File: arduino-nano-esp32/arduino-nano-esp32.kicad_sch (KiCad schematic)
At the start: 1 part

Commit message: symbol lib
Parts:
- added RFM95W1: ~, maciek-lib:lora-adafruit, symbol maciek-symbols:adafruit-rfm95w
- added SW1, SW2: ~, maciek-lib:3x4 switch, symbol maciek-symbols:3x4_switch
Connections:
- net +3.3V: now also RFM95W1.9 (VIN)
- net GND: now also RFM95W1.8 (GND), SW1.2, SW2.1
- net at A1.B1: now also SW1.1
- net at A1.D2: now also SW2.2
- net at A1.D3: now also RFM95W1.1
- net at A1.D4: now also RFM95W1.2
- net at A1.D5: now also RFM95W1.3
- net at A1.D6: now also RFM95W1.4
- net at A1.D7: now also RFM95W1.5
- net at A1.D8: now also RFM95W1.6
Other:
- moved on the sheet: A1

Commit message: net class plus cleanup
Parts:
- RFM95W1: footprint maciek-lib:lora-adafruit -> lora-adafruit
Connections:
- no-connect marks 0 -> 28
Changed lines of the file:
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@@
 		(color 0 0 0 0)
 	)
+	(no_connect
+		(at 143.51 59.69)
+	)
+	(no_connect
+		(at 113.03 40.64)
+	)
+	(no_connect
+		(at 97.79 66.04)
+	)
+	(no_connect
+		(at 46.99 93.98)
+	)
+	(no_connect
+		(at 46.99 81.28)
+	)
+	(no_connect
+		(at 143.51 62.23)
+	)
+	(no_connect
+		(at 97.79 53.34)
+	)
+	(no_connect
+		(at 113.03 121.92)
+	)
+	(no_connect
+		(at 97.79 71.12)
+	)
+	(no_connect
+		(at 46.99 66.04)
+	)
+	(no_connect
+		(at 46.99 71.12)
+	)
+	(no_connect
+		(at 123.19 64.77)
+	)
+	(no_connect
+		(at 97.79 68.58)
+	)
+	(no_connect
+		(at 97.79 73.66)
+	)
+	(no_connect
+		(at 97.79 55.88)
+	)
+	(no_connect
+		(at 97.79 76.2)
+	)
+	(no_connect
+		(at 46.99 68.58)
+	)
+	(no_connect
+		(at 143.51 69.85)
+	)
+	(no_connect
+		(at 143.51 64.77)
+	)
+	(no_connect
+		(at 143.51 67.31)
+	)
+	(no_connect
+		(at 46.99 78.74)
+	)
+	(no_connect
+		(at 46.99 83.82)
+	)
+	(no_connect
+		(at 46.99 73.66)
+	)
+	(no_connect
+		(at 113.03 111.76)
+	)
+	(no_connect
+		(at 46.99 91.44)
+	)
+	(no_connect
+		(at 46.99 58.42)
+	)
+	(no_connect
+		(at 46.99 76.2)
+	)
+	(no_connect
+		(at 113.03 50.8)
+	)
 	(wire
 		(pts
@@
 			(width 0)
 			(type default)
+		)
+	)
+	(netclass_flag ""
+		(length 2.54)
+		(shape round)
+		(at 33.02 105.41 90)
+		(fields_autoplaced yes)
+		(effects
+			(font
+				(size 1.27 1.27)
+			)
+			(justify left bottom)
+		)
+		(property "Netclass" "POWER"
+			(at 30.48 104.7115 90)
+			(effects
+				(font
+					(size 1.27 1.27)
+					(italic yes)
+				)
+				(justify left)
+			)
+		)
+	)
+	(netclass_flag ""
+		(length 2.54)
+		(shape round)
+		(at 25.4 44.45 90)
+		(fields_autoplaced yes)
+		(effects
+			(font
+				(size 1.27 1.27)
+			)
+			(justify left bottom)
+		)
+		(property "Netclass" "POWER"
+			(at 22.86 43.7515 90)
+			(effects
+				(font
+					(size 1.27 1.27)
+					(italic yes)
+				)
+				(justify left)
+			)
 		)
 	)
@@
 			)
 		)
-		(property "Footprint" "maciek-lib:lora-adafruit"
+		(property "Footprint" "lora-adafruit"
 			(at 142.24 80.01 0)
 			(effects

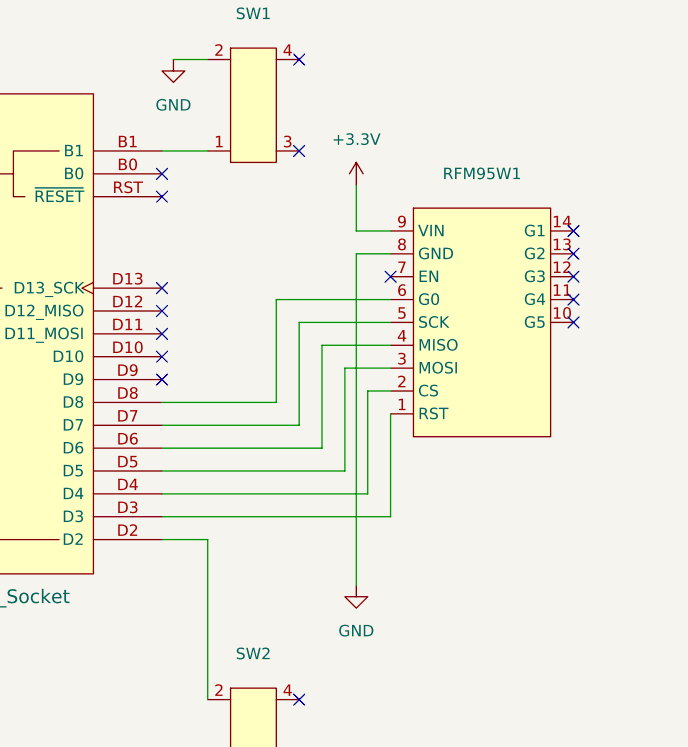
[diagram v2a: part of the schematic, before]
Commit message: add nests and 3v3 area
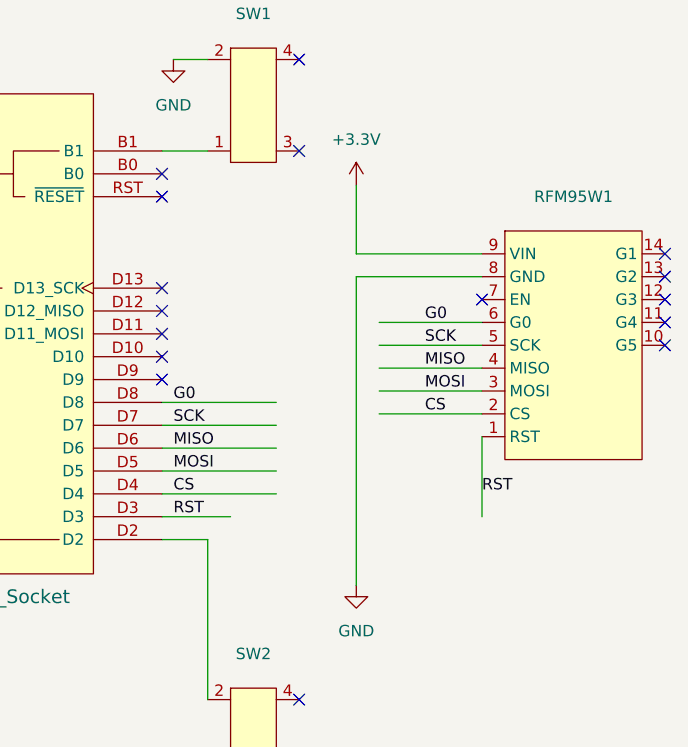
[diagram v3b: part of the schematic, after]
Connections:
- net RST: now reaches A1.D3, RFM95W1.1 (RST)
- net CS: now reaches A1.D4, RFM95W1.2 (CS)
- net MOSI: now reaches A1.D5, RFM95W1.3 (MOSI)
- net MISO: now reaches A1.D6, RFM95W1.4 (MISO)
- net SCK: now reaches A1.D7, RFM95W1.5 (SCK)
- net G0: now reaches A1.D8, RFM95W1.6 (G0)
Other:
- moved on the sheet: RFM95W1
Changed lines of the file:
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@@
 	)
 	(no_connect
-		(at 143.51 59.69)
+		(at 153.67 62.23)
 	)
 	(no_connect
@@
 	)
 	(no_connect
-		(at 143.51 62.23)
+		(at 153.67 64.77)
 	)
 	(no_connect
@@
 	)
 	(no_connect
-		(at 123.19 64.77)
+		(at 133.35 67.31)
 	)
 	(no_connect
@@
 	)
 	(no_connect
-		(at 143.51 69.85)
-	)
-	(no_connect
-		(at 143.51 64.77)
-	)
-	(no_connect
-		(at 143.51 67.31)
+		(at 153.67 72.39)
+	)
+	(no_connect
+		(at 153.67 67.31)
+	)
+	(no_connect
+		(at 153.67 69.85)
 	)
 	(no_connect
@@
 	(wire
 		(pts
-			(xy 110.49 67.31) (xy 123.19 67.31)
+			(xy 121.92 69.85) (xy 133.35 69.85)
 		)
 		(stroke
@@
 	(wire
 		(pts
-			(xy 97.79 81.28) (xy 113.03 81.28)
-		)
-		(stroke
-			(width 0)
-			(type default)
-		)
-	)
-	(wire
-		(pts
-			(xy 115.57 83.82) (xy 115.57 72.39)
+			(xy 97.79 81.28) (xy 110.49 81.28)
 		)
 		(stroke
@@
 	(wire
 		(pts
-			(xy 97.79 91.44) (xy 123.19 91.44)
-		)
-		(stroke
-			(width 0)
-			(type default)
-		)
-	)
-	(wire
-		(pts
-			(xy 118.11 86.36) (xy 118.11 74.93)
-		)
-		(stroke
-			(width 0)
-			(type default)
-		)
-	)
-	(wire
-		(pts
 			(xy 102.87 93.98) (xy 97.79 93.98)
 		)
@@
 	(wire
 		(pts
-			(xy 123.19 91.44) (xy 123.19 80.01)
-		)
-		(stroke
-			(width 0)
-			(type default)
-		)
-	)
-	(wire
-		(pts
-			(xy 110.49 78.74) (xy 110.49 67.31)
-		)
-		(stroke
-			(width 0)
-			(type default)
-		)
-	)
-	(wire
-		(pts
 			(xy 33.02 48.26) (xy 46.99 48.26)
 		)
@@
 	(wire
 		(pts
-			(xy 119.38 62.23) (xy 119.38 99.06)
-		)
-		(stroke
-			(width 0)
-			(type default)
-		)
-	)
-	(wire
-		(pts
-			(xy 113.03 69.85) (xy 123.19 69.85)
+			(xy 119.38 64.77) (xy 119.38 99.06)
+		)
+		(stroke
+			(width 0)
+			(type default)
+		)
+	)
+	(wire
+		(pts
+			(xy 121.92 72.39) (xy 133.35 72.39)
 		)
 		(stroke
@@
 	(wire
 		(pts
-			(xy 97.79 88.9) (xy 120.65 88.9)
+			(xy 97.79 88.9) (xy 110.49 88.9)
 		)
 		(stroke
@@
 	(wire
 		(pts
-			(xy 119.38 59.69) (xy 119.38 54.61)
+			(xy 119.38 62.23) (xy 119.38 54.61)
 		)
 		(stroke
@@
 	(wire
 		(pts
-			(xy 97.79 83.82) (xy 115.57 83.82)
-		)
-		(stroke
-			(width 0)
-			(type default)
-		)
-	)
-	(wire
-		(pts
-			(xy 113.03 81.28) (xy 113.03 69.85)
-		)
-		(stroke
-			(width 0)
-			(type default)
-		)
-	)
-	(wire
-		(pts
-			(xy 120.65 77.47) (xy 123.19 77.47)
-		)
-		(stroke
-			(width 0)
-			(type default)
-		)
-	)
-	(wire
-		(pts
-			(xy 115.57 72.39) (xy 123.19 72.39)
-		)
-		(stroke
-			(width 0)
-			(type default)
-		)
-	)
-	(wire
-		(pts
-			(xy 120.65 88.9) (xy 120.65 77.47)
-		)
-		(stroke
-			(width 0)
-			(type default)
-		)
-	)
-	(wire
-		(pts
-			(xy 118.11 74.93) (xy 123.19 74.93)
+			(xy 97.79 83.82) (xy 110.49 83.82)
+		)
+		(stroke
+			(width 0)
+			(type default)
+		)
+	)
+	(wire
+		(pts
+			(xy 121.92 80.01) (xy 133.35 80.01)
+		)
+		(stroke
+			(width 0)
+			(type default)
+		)
+	)
+	(wire
+		(pts
+			(xy 121.92 74.93) (xy 133.35 74.93)
+		)
+		(stroke
+			(width 0)
+			(type default)
+		)
+	)
+	(wire
+		(pts
+			(xy 121.92 77.47) (xy 133.35 77.47)
 		)
 		(stroke
@@
 	(wire
 		(pts
-			(xy 123.19 62.23) (xy 119.38 62.23)
-		)
-		(stroke
-			(width 0)
-			(type default)
-		)
-	)
-	(wire
-		(pts
-			(xy 97.79 86.36) (xy 118.11 86.36)
-		)
-		(stroke
-			(width 0)
-			(type default)
-		)
-	)
-	(wire
-		(pts
-			(xy 123.19 59.69) (xy 119.38 59.69)
+			(xy 133.35 91.44) (xy 133.35 82.55)
+		)
+		(stroke
+			(width 0)
+			(type default)
+		)
+	)
+	(wire
+		(pts
+			(xy 133.35 64.77) (xy 119.38 64.77)
+		)
+		(stroke
+			(width 0)
+			(type default)
+		)
+	)
+	(wire
+		(pts
+			(xy 97.79 86.36) (xy 110.49 86.36)
+		)
+		(stroke
+			(width 0)
+			(type default)
+		)
+	)
+	(wire
+		(pts
+			(xy 105.41 91.44) (xy 97.79 91.44)
+		)
+		(stroke
+			(width 0)
+			(type default)
+		)
+	)
+	(wire
+		(pts
+			(xy 133.35 62.23) (xy 119.38 62.23)
 		)
 		(stroke
@@
 			(width 0)
 			(type default)
+		)
+	)
+	(label "RST"
+		(at 99.06 91.44 0)
+		(fields_autoplaced yes)
+		(effects
+			(font
+				(size 1.27 1.27)
+			)
+			(justify left bottom)
+		)
+	)
+	(label "SCK"
+		(at 127 72.39 0)
+		(fields_autoplaced yes)
+		(effects
+			(font
+				(size 1.27 1.27)
+			)
+			(justify left bottom)
+		)
+	)
+	(label "MISO"
+		(at 127 74.93 0)
+		(fields_autoplaced yes)
+		(effects
+			(font
+				(size 1.27 1.27)
+			)
+			(justify left bottom)
+		)
+	)
+	(label "MISO"
+		(at 99.06 83.82 0)
+		(fields_autoplaced yes)
+		(effects
+			(font
+				(size 1.27 1.27)
+			)
+			(justify left bottom)
+		)
+	)
+	(label "SCK"
+		(at 99.06 81.28 0)
+		(fields_autoplaced yes)
+		(effects
+			(font
+				(size 1.27 1.27)
+			)
+			(justify left bottom)
+		)
+	)
+	(label "MOSI"
+		(at 99.06 86.36 0)
+		(fields_autoplaced yes)
+		(effects
+			(font
+				(size 1.27 1.27)
+			)
+			(justify left bottom)
+		)
+	)
+	(label "CS"
+		(at 99.06 88.9 0)
+		(fields_autoplaced yes)
+		(effects
+			(font
+				(size 1.27 1.27)
+			)
+			(justify left bottom)
+		)
+	)
+	(label "CS"
+		(at 127 80.01 0)
+		(fields_autoplaced yes)
+		(effects
+			(font
+				(size 1.27 1.27)
+			)
+			(justify left bottom)
+		)
+	)
+	(label "RST"
+		(at 133.35 88.9 0)
+		(fields_autoplaced yes)
+		(effects
+			(font
+				(size 1.27 1.27)
+			)
+			(justify left bottom)
+		)
+	)
+	(label "G0"
+		(at 99.06 78.74 0)
+		(fields_autoplaced yes)
+		(effects
+			(font
+				(size 1.27 1.27)
+			)
+			(justify left bottom)
+		)
+	)
+	(label "G0"
+		(at 127 69.85 0)
+		(fields_autoplaced yes)
+		(effects
+			(font
+				(size 1.27 1.27)
+			)
+			(justify left bottom)
+		)
+	)
+	(label "MOSI"
+		(at 127 77.47 0)
+		(fields_autoplaced yes)
+		(effects
+			(font
+				(size 1.27 1.27)
+			)
+			(justify left bottom)
 		)
 	)
@@
 	(symbol
 		(lib_id "maciek-symbols:adafruit-rfm95w")
-		(at 133.35 69.85 0)
+		(at 143.51 72.39 0)
 		(unit 1)
 		(exclude_from_sim no)
@@
 		(fields_autoplaced yes)
 		(property "Reference" "RFM95W1"
-			(at 133.35 53.34 0)
+			(at 143.51 55.88 0)
 			(effects
 				(font
@@
 		)
 		(property "Value" "~"
-			(at 133.35 55.88 0)
+			(at 143.51 58.42 0)
 			(effects
 				(font
@@
 		)
 		(property "Footprint" "lora-adafruit"
-			(at 142.24 80.01 0)
+			(at 152.4 82.55 0)
 			(effects
 				(font
@@
 		)
 		(property "Datasheet" ""
-			(at 142.24 80.01 0)
+			(at 152.4 82.55 0)
 			(effects
 				(font
@@
 		)
 		(property "Description" ""
-			(at 142.24 80.01 0)
-			(effects
-				(font
+			(at 152.4 82.55 0)
+			(effects
+				(font

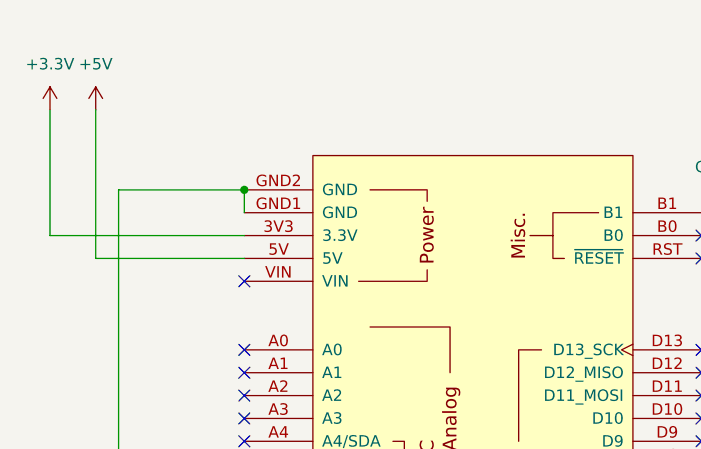
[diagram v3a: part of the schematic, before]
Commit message: need bigger holes
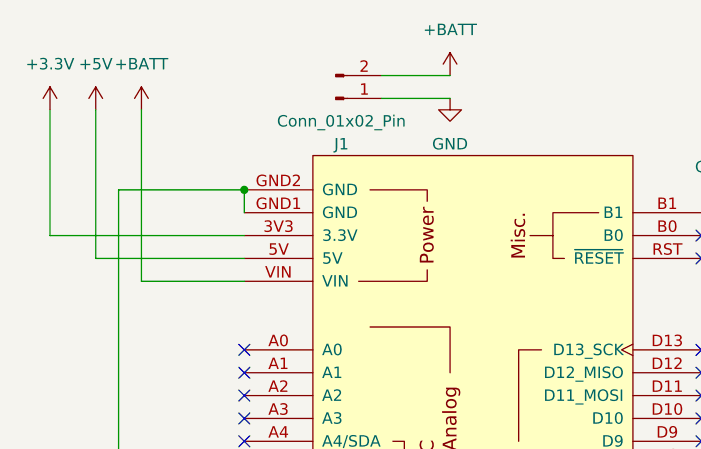
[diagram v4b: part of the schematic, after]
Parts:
- added J1: Conn_01x02_Pin, Connector_PinHeader_2.54mm:PinHeader_1x02_P2.54mm_Horizontal, symbol Connector:Conn_01x02_Pin
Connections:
- net GND: now also J1.1 (Pin_1)
- net +BATT: now reaches A1.VIN
- net +BATT: now also J1.2 (Pin_2)
- no-connect marks 28 -> 27
